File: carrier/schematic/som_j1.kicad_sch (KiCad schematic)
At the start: 1 part, among them J1701 DF40C-100DS-0.4V(51)

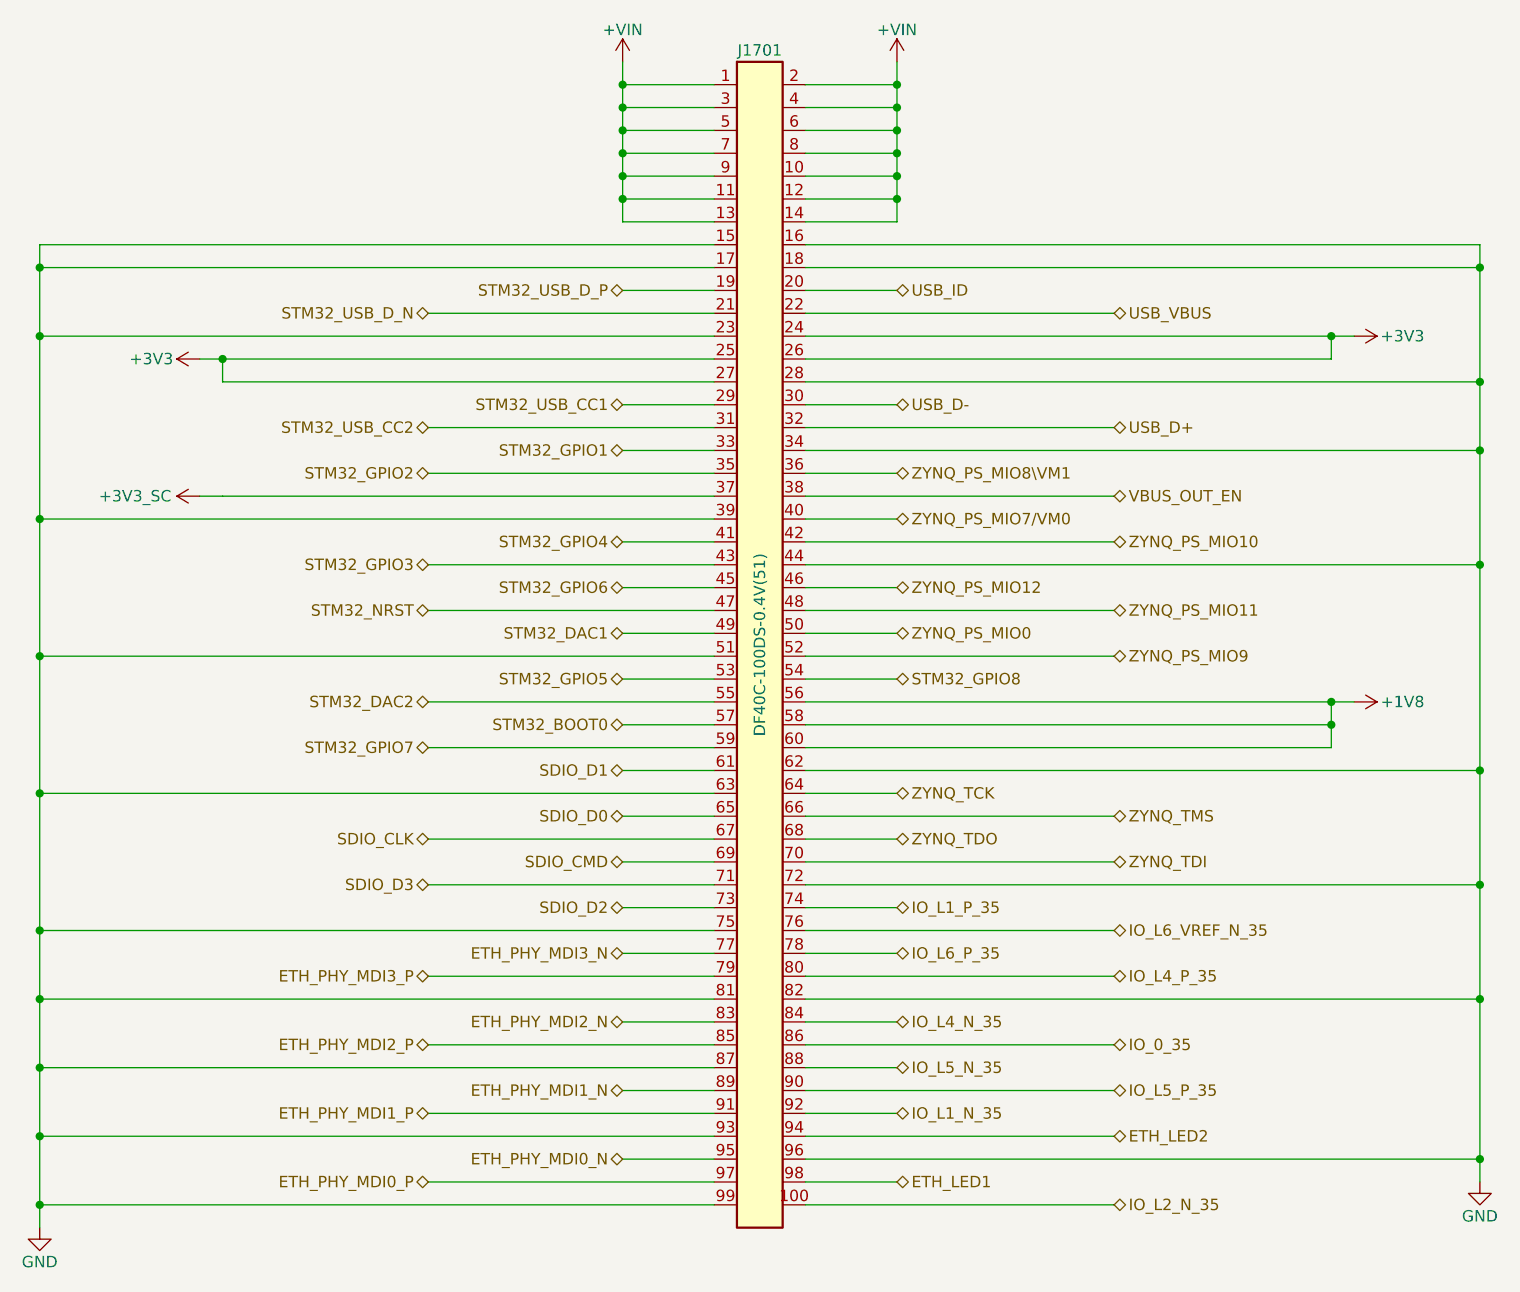
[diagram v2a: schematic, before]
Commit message: som_j1: SoM RAIL ISOLATION (PLAN round 5) — +3V3/+1V8 J1 pins explicit author NCs
The SoM exports its own +3V3 (J1.24-27) / +1V8 (J1.56/58/60) from on-module
MPM3834 stages while carrier power.py regulates the same-named rails —
binding them would parallel two regulators on one net. Carrier bucks WIN:

- carrier/som_conn_gen.py: declarative ISOLATED_SOM_RAILS map (rationale
  per rail) — isolated pins are emitted as explicit per-pin no-connects,
  never silently dropped; the per-sheet netlist gate proves all 7 NCs.
- schgen/link.py: ISOLATED_SOM_RAILS policy twin next to RAIL_ALIASES; the
  rail census reports the isolation instead of a SoM bind, the rails no
  longer count as unbound contract nets, and the linker ERRORS if a
  connector sheet ever re-binds an isolated rail (mutation-tested: guard
  fires when the authoring map is blanked).
- schgen/place.py: connector-fan template handles author-NC pins
  generically (no-connect cross at the pin, no fan row — same idiom as the
  chain/fan templates).
- schgen/powertree.py: the PARALLEL-SOURCE finding logic was already
  netlist-driven, so it auto-clears; it stays (generalized to all som_j*
  sheets) as the guard that re-fires if the isolation is ever broken.

Root ERC 0, BOARD GATE PASS, POWER TREE PASS (findings 2 -> 1: only the
VBUS pre-contract flag remains, owned by the round-5 eFuse unit). som_j1
render eyeballed full-res (NC crosses on 24-27/56/58/60) and blessed.

Co-Authored-By: Claude Fable 5 <noreply@anthropic.com>
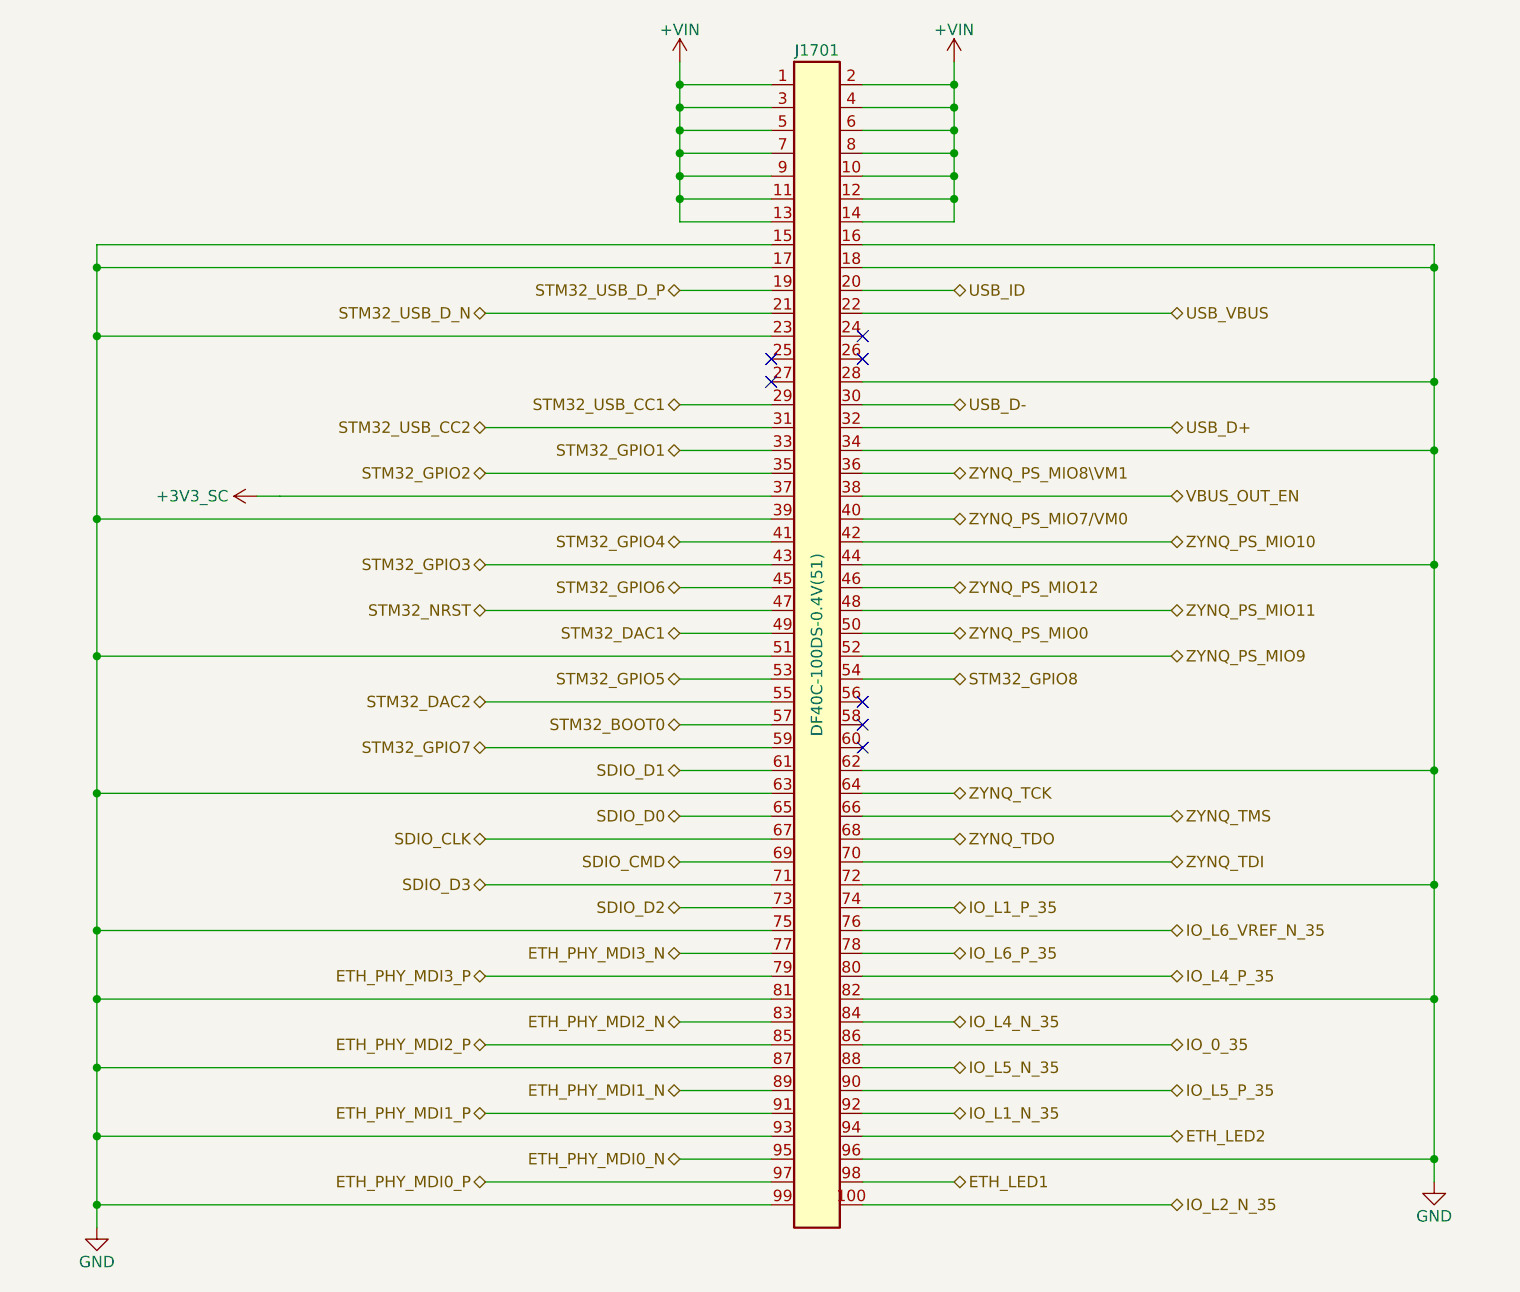
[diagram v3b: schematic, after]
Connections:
- removed net +1V8: J1701.56, J1701.58, J1701.60
- removed net +3V3: J1701.24, J1701.25, J1701.26, J1701.27
- no-connect marks 0 -> 7
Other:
- moved on the sheet: J1701

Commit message: som_j1: J1 VIN rebind +VIN(20V) -> +5V_SOM (P0 fix, UNIT 2)
The J1 VIN pins (J1.1-14, SoM net VIN) bound to the 20V PD rail +VIN —
the bug that destroys the 4.2-5V SoM at the first PD contract
(wave3_function_map.md P0). Rebound to the carrier always-on +5V_SOM buck
(power.py U4, UNIT 1), declaratively and never silently:

- carrier/som_conn_gen.py: REBOUND_SOM_RAILS {"VIN": "+5V_SOM"} documents
  the SoM-net -> carrier-rail rebind with rationale (same pattern as
  ISOLATED_SOM_RAILS); RAIL_SPELLING is derived from it. The J1 +VIN draw
  (0.5A "at 20V" — wrong twice over) becomes c.draws("+5V_SOM", 2.0,
  "SoM ~10W class at 5V") on the consuming connector (wave3 P0 point 2).
- schgen/link.py: REBOUND_SOM_RAILS policy twin (carrier rail -> SoM net)
  so the rail census accounts the 14 SoM VIN pins under +5V_SOM; canon_to_som
  consults it; RAIL_ALIASES drops the stale +VIN<->VIN entry. Two new drift
  guards (LAW 4 — strict, not soft): a "REBIND BROKEN/DRIFT" error if the
  rebound rail is absent from a connector sheet or the raw SoM net reappears
  there, and a "SoM OVERVOLTAGE" error if the 20V +VIN ever reaches a
  connector sheet. Link report prints the rebind in the alias section.

Gates: board PASS (23 sheets); root ERC 0; J1 render eyeballed — pins 1-14
now bus to two +5V_SOM flags, +VIN gone from J1, the +3V3/+1V8 round-5 NCs
intact (no overlap/crossing). Link census: "+5V_SOM — P0 REBIND of SoM
'VIN' -> 14 pins", +VIN now carrier-local (pd_input/power/power_mon only),
unbound SoM nets 0. Power tree 16 regs/0 findings: U4 +VIN->+5V_SOM
2.004A/3.0A (67%). m1_rc PASS; selftest 40/40 + determinism PASS; goldens
unchanged (label-only edit below the perceptual-hash threshold).

Co-Authored-By: Claude Fable 5 <noreply@anthropic.com>
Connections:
- net +VIN renamed +5V_SOM
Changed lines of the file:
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@@
 	)
 	(symbol
-		(lib_id "schgen:+VIN")
+		(lib_id "schgen:+5V_SOM")
 		(at 139.7 27.94 0)
 		(unit 1)
@@
 		(property
 			"Value"
-			"+VIN"
+			"+5V_SOM"
 			(at 139.7 24.384 0)
 			(effects
@@
 	)
 	(symbol
-		(lib_id "schgen:+VIN")
+		(lib_id "schgen:+5V_SOM")
 		(at 170.18 27.94 0)
 		(unit 1)
@@
 		(property
 			"Value"
-			"+VIN"
+			"+5V_SOM"
 			(at 170.18 24.384 0)
 			(effects

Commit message: audit-fix(engine): harvest F1-F7,F9 — gate hardening + leak + guards
F1 selftest now exercises the VISUAL gate against geometry mutants (wire-cross
+ text-over-wire) — proven to bite (was never run on a mutant before).
F2 visual_gate catches different-net wire T-touch / butt-join shorts.
F3 netlist_gate no longer leaks tmp .net files (was 2671 stale).
F4 board uniquify guards the stride (widened 100->1000) against ref collision.
F5 hier-mode sheets now re-run through the per-sheet netlist gate.
F6 dead clause dropped; F7 stale zynq_eda docstring fixed; F9 eager inline-pin
validation. Source copied verbatim from the audit-fix worktree (6 files, proven
untouched on origin since its base); board regenerated fresh. All gates green,
selftest geo-mutants killed by the visual gate, goldens 23/23, m1_rc PASS.

Co-Authored-By: Claude Fable 5 <noreply@anthropic.com>
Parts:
- renumbered J1701 to J17001
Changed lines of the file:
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@@
 		(property
 			"Reference"
-			"J1701"
+			"J17001"
 			(at 154.94 26.67 0)
 			(effects
@@
 				(path
 					"/c2797150-7a6e-556a-82f5-fdda13c31368/cb8332a7-7e9d-541e-92f8-4b378fa3e437"
-					(reference "J1701")
+					(reference "J17001")
 					(unit 1)
 				)
@@
 		(property
 			"Reference"
-			"#PWR1701"
+			"#PWR17001"
 			(at 139.7 25.4 0)
 			(effects
@@
 				(path
 					"/c2797150-7a6e-556a-82f5-fdda13c31368/cb8332a7-7e9d-541e-92f8-4b378fa3e437"
-					(reference "#PWR1701")
+					(reference "#PWR17001")
 					(unit 1)
 				)
@@
 		(property
 			"Reference"
-			"#PWR1702"
+			"#PWR17002"
 			(at 92.71 73.66 0)
 			(effects
@@
 				(path
 					"/c2797150-7a6e-556a-82f5-fdda13c31368/cb8332a7-7e9d-541e-92f8-4b378fa3e437"
-					(reference "#PWR1702")
+					(reference "#PWR17002")
 					(unit 1)
 				)
@@
 		(property
 			"Reference"
-			"#PWR1703"
+			"#PWR17003"
 			(at 74.93 154.94 0)
 			(effects
@@
 				(path
 					"/c2797150-7a6e-556a-82f5-fdda13c31368/cb8332a7-7e9d-541e-92f8-4b378fa3e437"
-					(reference "#PWR1703")
+					(reference "#PWR17003")
 					(unit 1)
 				)
@@
 		(property
 			"Reference"
-			"#PWR1704"
+			"#PWR17004"
 			(at 170.18 25.4 0)
 			(effects
@@
 				(path
 					"/c2797150-7a6e-556a-82f5-fdda13c31368/cb8332a7-7e9d-541e-92f8-4b378fa3e437"
-					(reference "#PWR1704")
+					(reference "#PWR17004")
 					(unit 1)
 				)
@@
 		(property
 			"Reference"
-			"#PWR1705"
+			"#PWR17005"
 			(at 223.52 149.86 0)
 			(effects
@@
 				(path
 					"/c2797150-7a6e-556a-82f5-fdda13c31368/cb8332a7-7e9d-541e-92f8-4b378fa3e437"
-					(reference "#PWR1705")
+					(reference "#PWR17005")
 					(unit 1)
 				)
